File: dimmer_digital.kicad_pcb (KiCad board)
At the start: 2 copper layers, 81.3 x 55.9 mm, 26 parts, among them J1 AVR-ISP-6, J2 CONECTOR_LEFT, J3 CONNECTOR_SPEED, J4 TERMINAL_AC, J5 TERMINAL_LOAD, J6 CONECTOR_RIGHT, Q1 TIC226, SW1 SW_DPDT_x2, SW2 SW_Push, U1 ATtiny13A-PU, U2 MOC3021M, U3 4N25

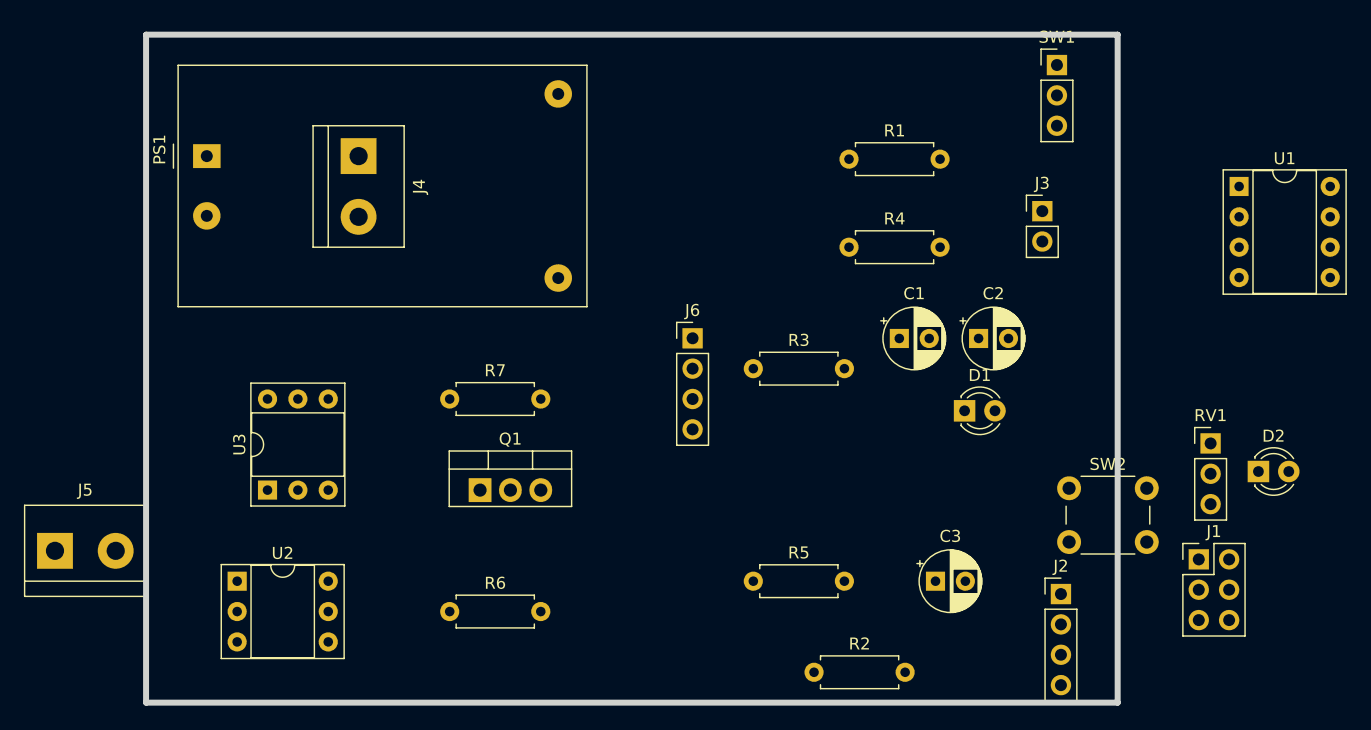
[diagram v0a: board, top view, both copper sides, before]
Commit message: positioning AC side
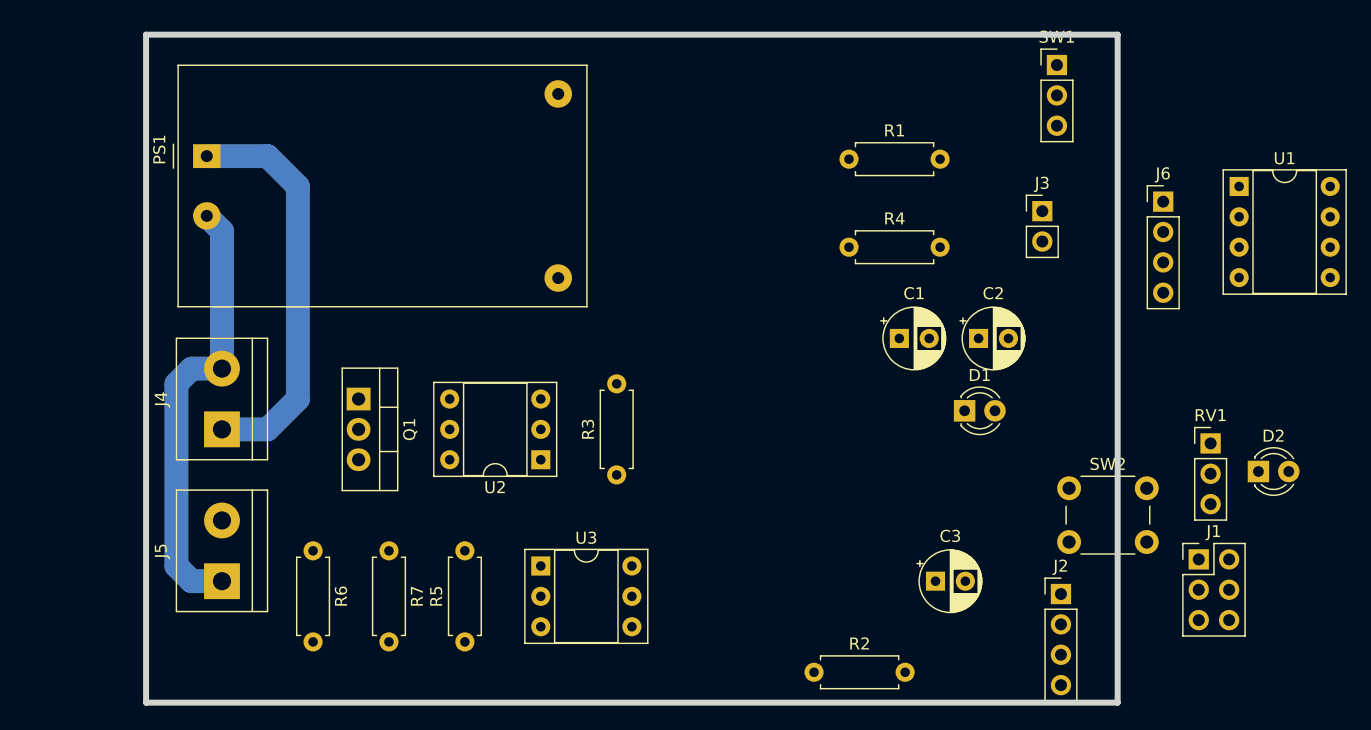
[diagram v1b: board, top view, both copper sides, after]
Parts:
- moved J6 41.0 mm to (135.9, 39.4)
- moved U2 27.4 mm to (83.8, 61.0), turned to 180 degrees
- moved J4 25.6 mm to (57.1, 58.4), turned to 90 degrees
- moved R5 24.7 mm to (77.5, 76.2), turned to 90 degrees
- moved U3 23.7 mm to (83.8, 69.8), turned to 0 degrees
- moved R3 14.5 mm to (90.2, 62.2), turned to 90 degrees
- moved J5 14.2 mm to (57.1, 71.1), turned to 90 degrees
- moved R7 13.7 mm to (71.1, 68.6), turned to 270 degrees
- moved Q1 12.7 mm to (68.6, 55.9), turned to 270 degrees
- moved R6 12.5 mm to (64.8, 68.6), turned to 270 degrees
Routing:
- net AC2: track 0.00 -> 37.2 mm
- net AC1: track 0.00 -> 33.9 mm
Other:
- net class Default: clearance 1 -> 0.2; trace_width 1 -> 0.25; via_dia 1.5 -> 0.8; via_drill 1 -> 0.4
- net class POWER_AC removed
- net class POWER_DC removed
- net class PWR_AC added: clearance 0.5, trace_width 2, via_dia 1.2, via_drill 1
- net class PWR_DC added: clearance 0.5, trace_width 1.5, via_dia 1.2, via_drill 1
- net class Signals added: clearance 0.5, trace_width 1, via_dia 1.2, via_drill 1
- rule trace_clearance: 1 -> 0.2
- rule trace_min: 1 -> 0.2
- rule via_min_drill: 1 -> 0.3
- rule via_min_size: 1 -> 0.4

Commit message: wiring AC side
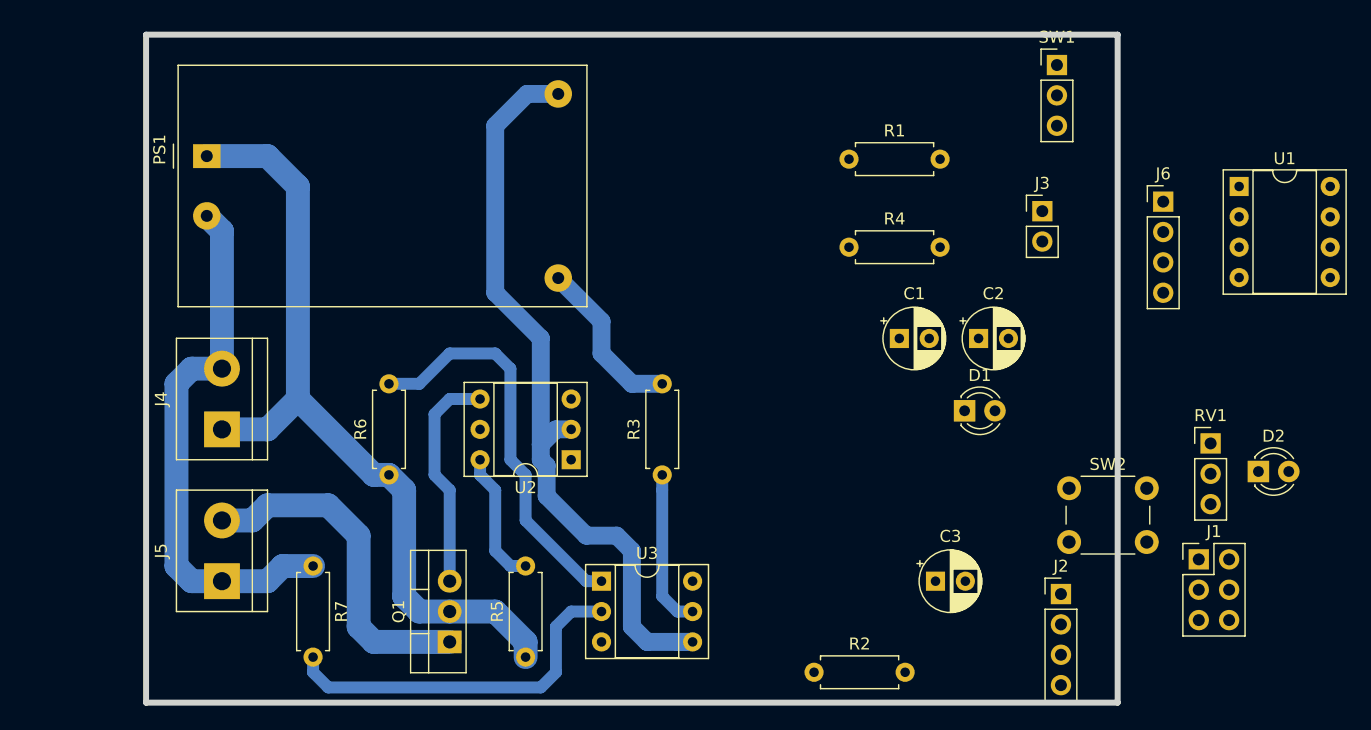
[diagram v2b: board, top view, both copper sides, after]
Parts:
- moved Q1 21.7 mm to (76.2, 76.2), turned to 90 degrees
- moved R6 8.98 mm to (71.1, 62.2), turned to 90 degrees
- moved R7 6.48 mm to (64.8, 69.8)
- moved U3 5.24 mm to (88.9, 71.1)
- moved R5 5.24 mm to (82.5, 77.5)
- moved R3 3.81 mm to (94.0, 62.2)
- moved U2 2.54 mm to (86.4, 61.0)
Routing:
- net GND: track 0.00 -> 64.4 mm
- net AC1: track 33.9 -> 67.8 mm
- net Net-(R6-Pad2): track 0.00 -> 33.4 mm
- net Net-(R7-Pad2): track 0.00 -> 30.8 mm
- net LOAD2: track 0.00 -> 28.8 mm
- net Net-(Q1-Pad3): track 0.00 -> 18.8 mm
- net +5V: track 0.00 -> 13.9 mm
- net CROSSOVER: track 0.00 -> 13.2 mm
- net Net-(R5-Pad2): track 0.00 -> 11.2 mm
- net AC2: track 37.2 -> 45.4 mm

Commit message: wiring complete
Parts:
- removed J1: AVR-ISP-6, Connector_PinHeader_2.54mm:PinHeader_2x03_P2.54mm_Vertical
- SW1: value SW_DPDT_x2 -> SWITCH_SPEED
- moved J2 49.5 mm to (102.9, 29.2), turned to 270 degrees
- moved U1 39.7 mm to (102.9, 33.0), turned to 270 degrees
- moved J6 33.4 mm to (102.9, 44.5), turned to 270 degrees
- moved R2 29.5 mm to (102.9, 49.5), turned to 180 degrees
- moved SW2 28.2 mm to (123.2, 35.6), turned to 90 degrees
- moved D2 27.2 mm to (116.8, 58.4), turned to 180 degrees
- moved C1 16.6 mm to (115.6, 34.3), turned to 270 degrees
- moved SW1 16.6 mm to (110.5, 29.2), turned to 90 degrees
- moved D1 16.4 mm to (102.9, 57.1), turned to 90 degrees
- moved RV1 13.8 mm to (127.0, 54.6), turned to 180 degrees
- moved C3 13.5 mm to (127.0, 62.2), turned to 90 degrees
- moved R4 10.4 mm to (111.8, 53.3)
- moved C2 9.06 mm to (115.6, 43.2), turned to 90 degrees
- moved R1 6.11 mm to (109.2, 41.9), turned to 90 degrees
- moved J3 4.46 mm to (127.0, 44.5), turned to 180 degrees
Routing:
- net GND: track 64.4 -> 203.0 mm
- net +5V: track 13.9 -> 96.9 mm
- net Net-(RV1-Pad2): track 0.00 -> 39.0 mm
- net CROSSOVER: track 13.2 -> 51.9 mm
- net AC2: track 45.4 -> 76.5 mm
- net RESET: track 0.00 -> 27.9 mm
- net SPEED_POT: track 0.00 -> 22.6 mm
- net SPEED_EXTERNAL: track 0.00 -> 22.5 mm
- net Net-(D1-Pad1): track 0.00 -> 18.1 mm
- net Net-(C2-Pad1): track 0.00 -> 15.3 mm
- net LOAD2: track 28.8 -> 43.8 mm
- net AC1: track 67.8 -> 81.6 mm
- net Net-(C1-Pad1): track 0.00 -> 11.2 mm
- net PHASE_CONTROL: track 0.00 -> 8.89 mm
- net Net-(D2-Pad2): track 0.00 -> 6.13 mm
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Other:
- board size 81.3 x 55.9 mm -> 82.5 x 55.9 mm

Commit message: Finished Rev0
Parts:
- added G***: LOGO, igorkelvin:Logo_Cefet_10mm, F.Cu at (71.1, 36.8)
- added REF**: PinHeader_2x10_P2.54mm_Vertical, Connector_PinHeader_2.54mm:PinHeader_2x10_P2.54mm_Vertical, F.Cu at (104.1, 71.1)
- added REF**: PinHeader_2x10_P2.54mm_Vertical, Connector_PinHeader_2.54mm:PinHeader_2x10_P2.54mm_Vertical, F.Cu at (104.1, 77.5)
- J3: value CONNECTOR_SPEED -> CON_SPEED
- moved D1 1.80 mm to (104.1, 58.4), turned to 180 degrees
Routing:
- net GND: track 203.0 -> 218.7 mm
- net +5V: track 96.9 -> 109.6 mm
- net AC2: track 76.5 -> 87.2 mm
- net CROSSOVER: track 51.9 -> 57.0 mm
- net Net-(D1-Pad2): track 5.08 -> 9.42 mm
- net Net-(D1-Pad1): track 18.1 -> 20.4 mm
- net AC1: track 81.6 -> 83.3 mm
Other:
- board text added: "Dimmer c/ ATtiny13 - Rev 0 Igor Kelvin <igorkelvin@gmail.com> 2020-07-11"

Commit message: Visual update on the schematic
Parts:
- J3: value CON_SPEED -> CONNECTOR_SPEED

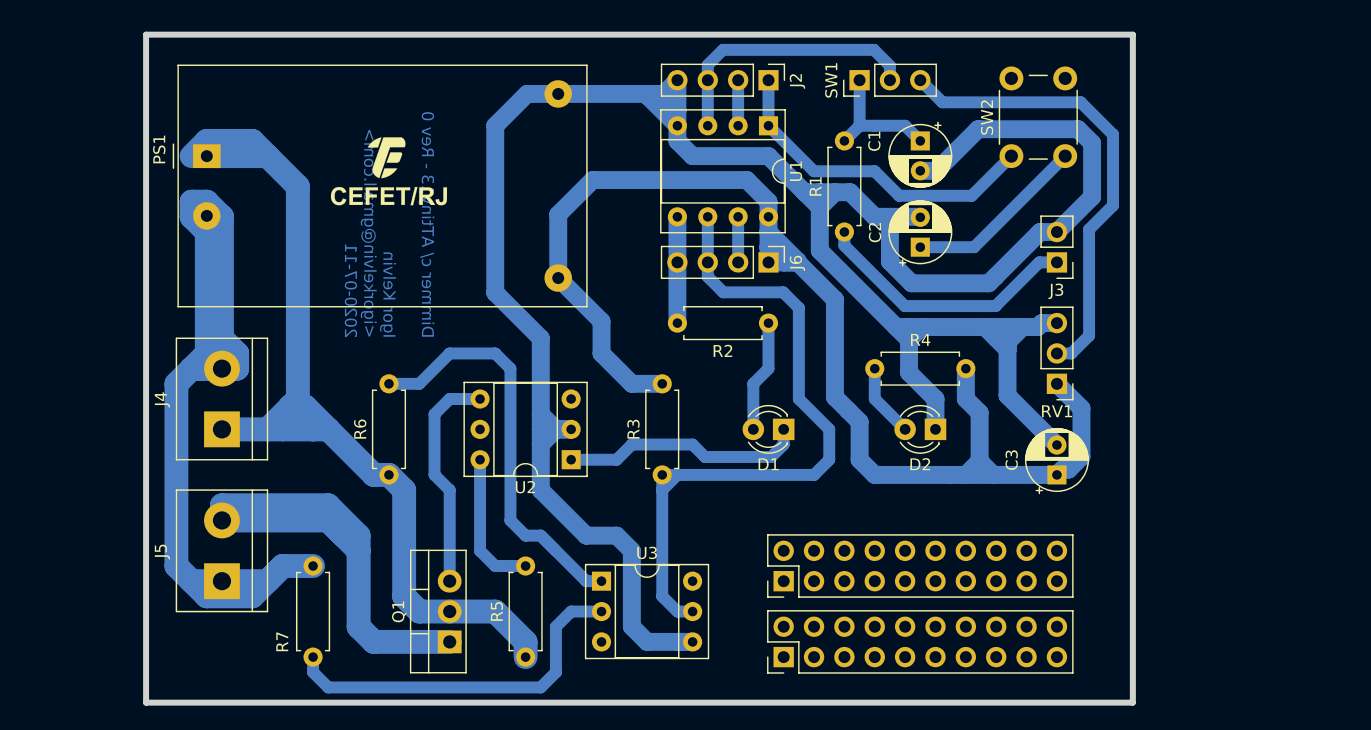
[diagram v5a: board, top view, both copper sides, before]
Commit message: add screw mount holes
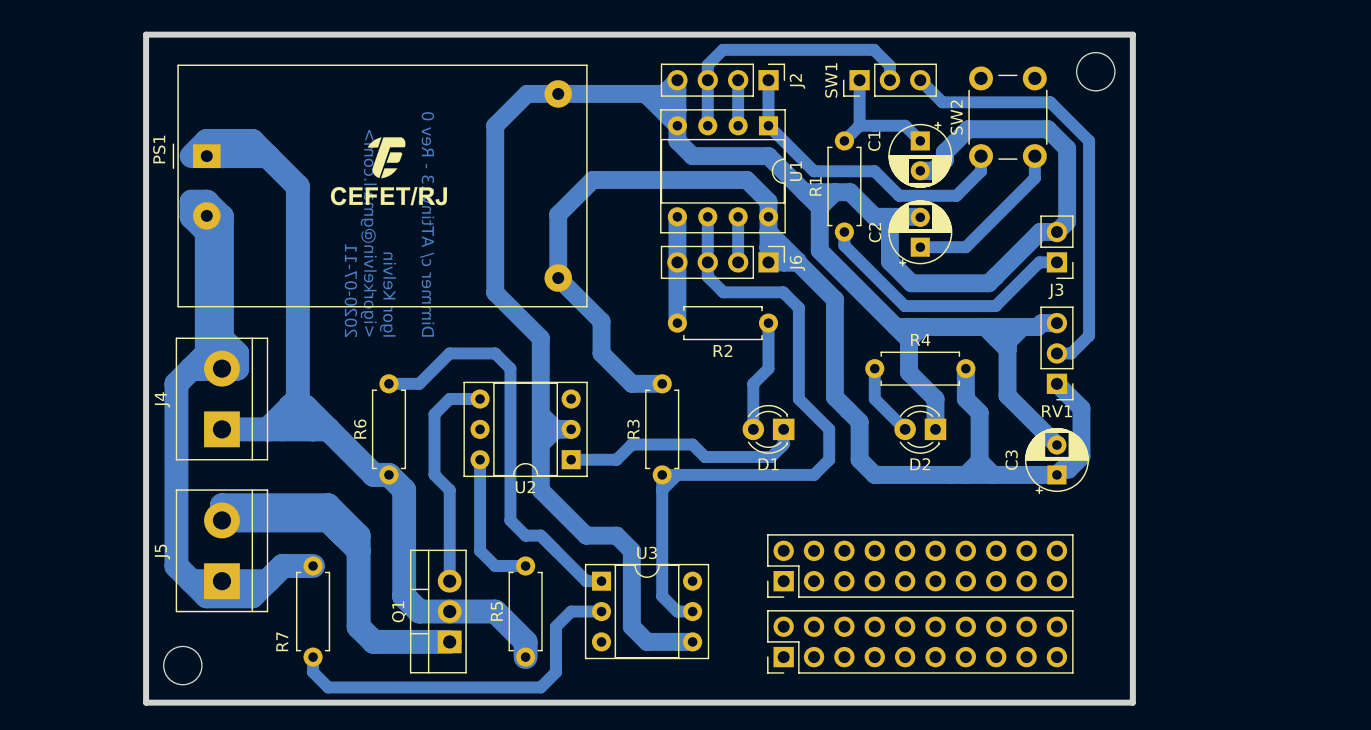
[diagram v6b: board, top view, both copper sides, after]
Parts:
- moved SW2 2.54 mm to (120.7, 35.6)
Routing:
- net Net-(RV1-Pad2): track 39.0 -> 35.8 mm
- net RESET: track 27.9 -> 26.1 mm
- net GND: track 218.7 -> 217.2 mm
- net Net-(C2-Pad1): track 15.3 -> 13.8 mm
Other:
- outline, holes or cut-outs redrawn
